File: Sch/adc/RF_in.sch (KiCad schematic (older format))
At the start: 72 parts, among them CN1 SMA, CN2 SMA, J3 JP2, J4 JP2, U1 LTC2292, U2 BGA2818

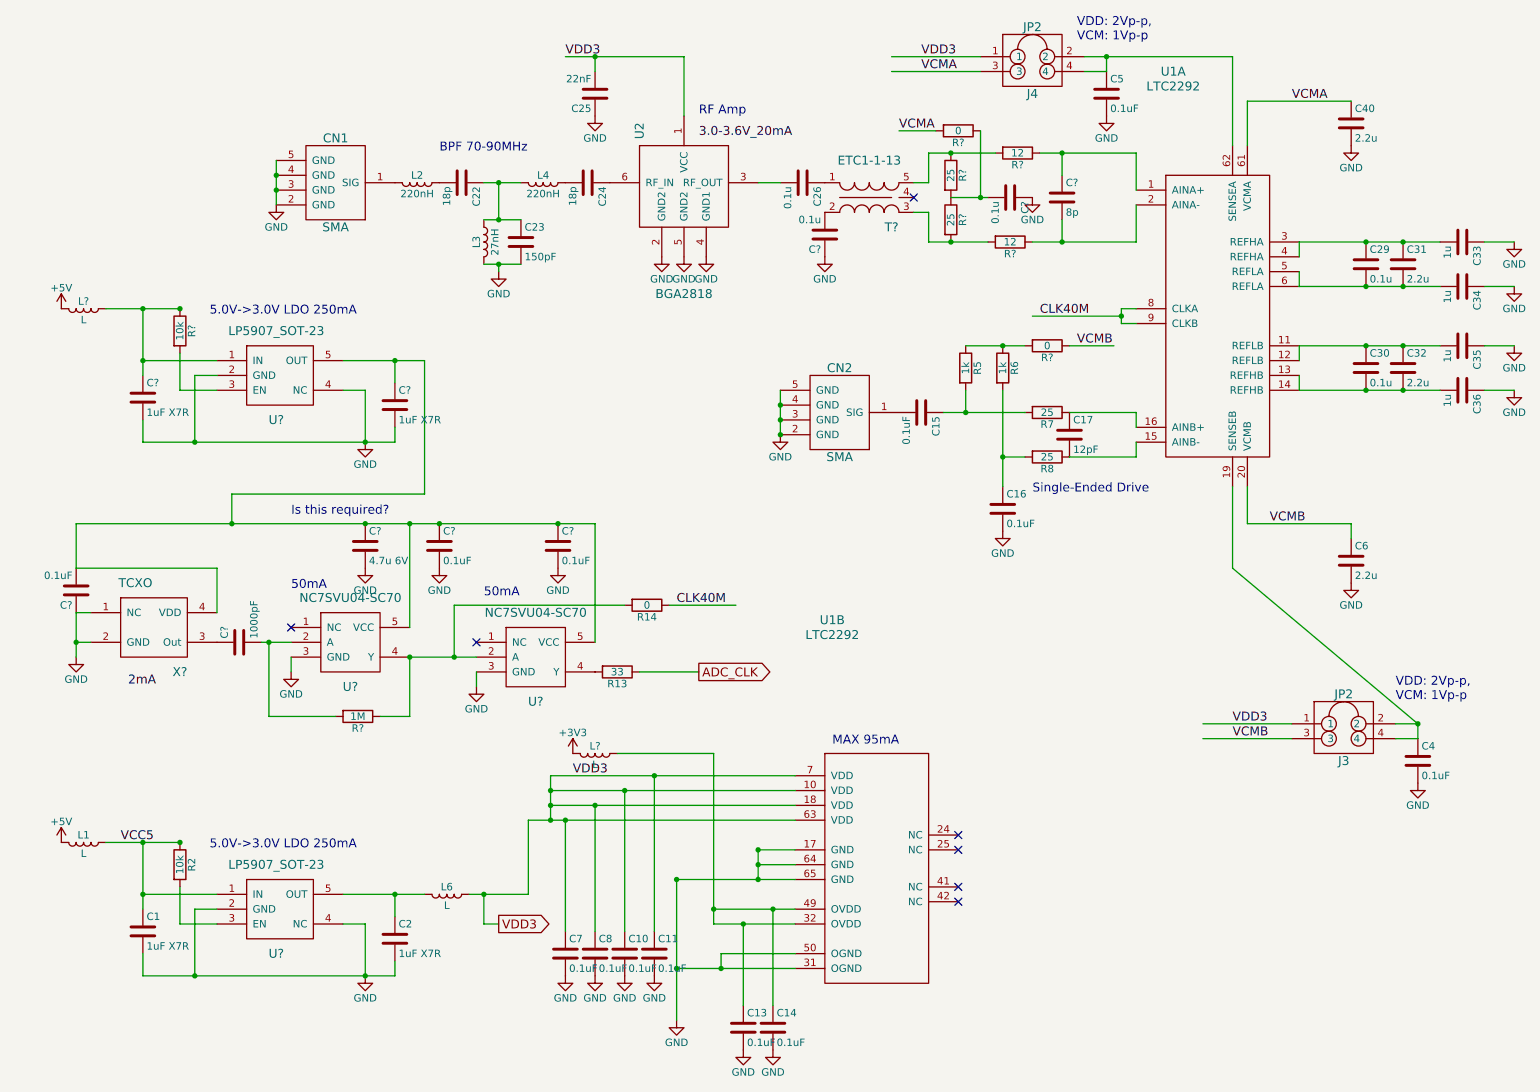
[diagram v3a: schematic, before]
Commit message: Analog front end is removed from the ADC board. ADC board is done
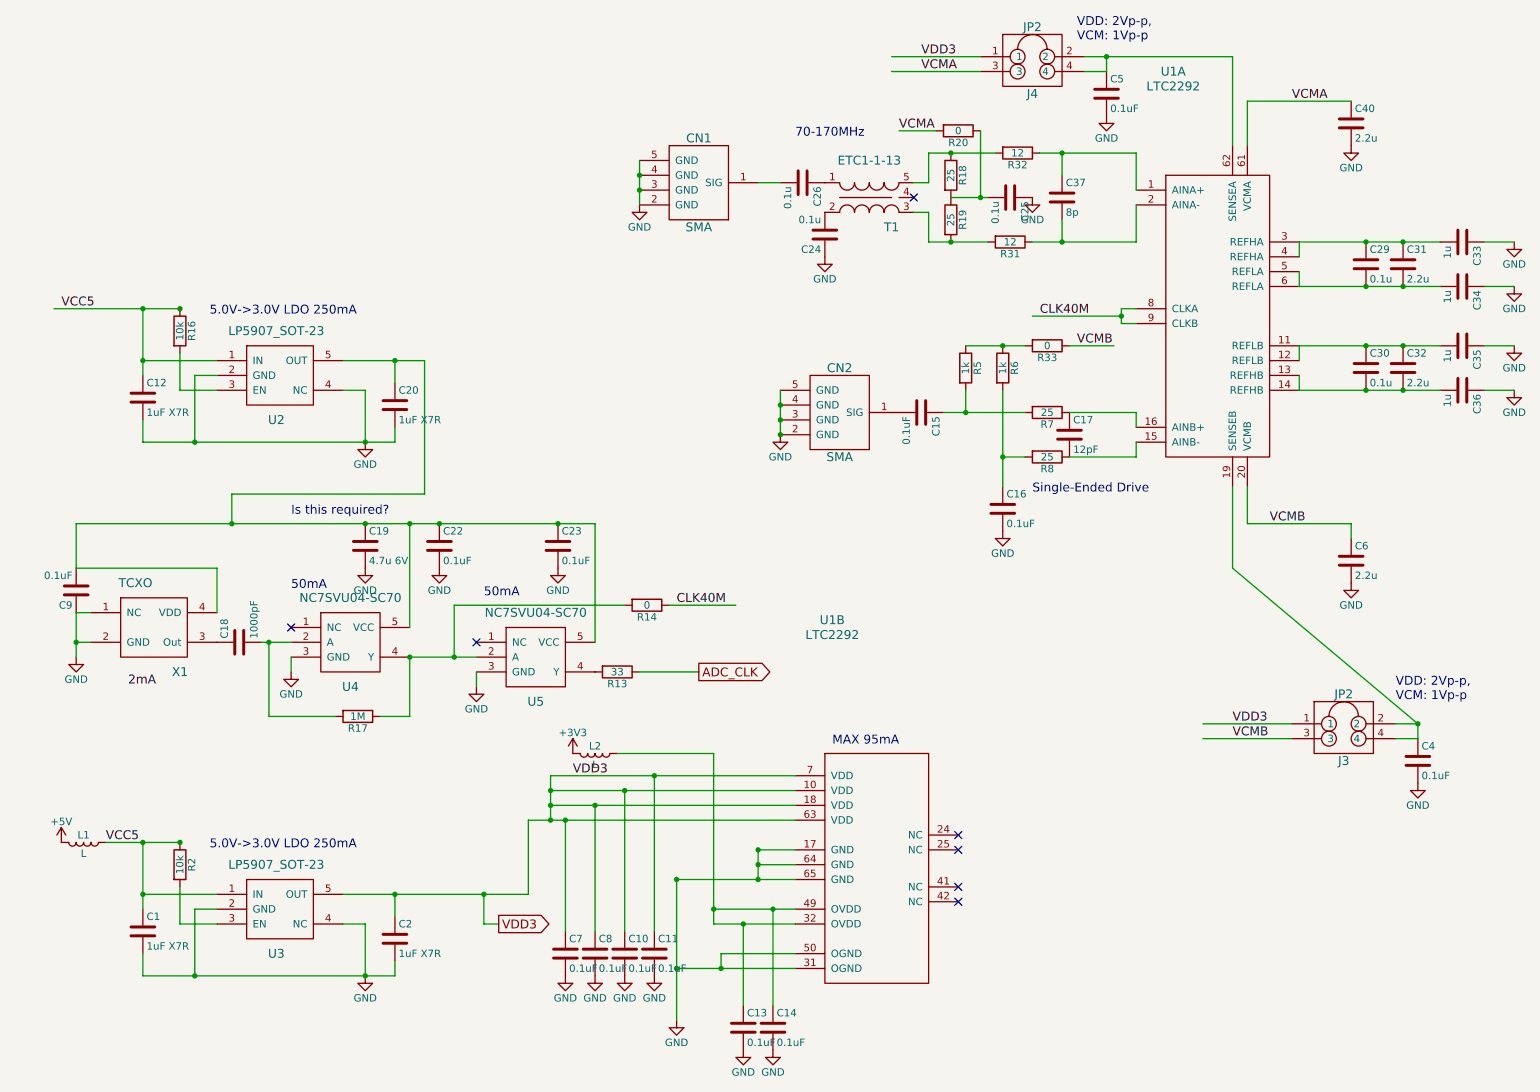
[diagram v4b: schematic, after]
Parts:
- removed C22, C24: 18p, adc_lib:C0603, symbol C
- removed C23: 150pF, adc_lib:C0603, symbol C
- removed C25: 22nF, adc_lib:C0603, symbol C
- removed L2, L4: 220nH, adc_lib:L0603, symbol L
- removed L3: 27nH, adc_lib:L0603, symbol L
- removed L6, L?: L, adc_lib:FB0805, symbol L
- removed U2: BGA2818, adc_lib:BGA2818, symbol BGA2818
- gave numbers to parts that had none: 25
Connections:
- net labels removed: 3.0-3.6V_20mA
- wire segments 149 -> 140
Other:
- note added: "70-170MHz"
- note removed: "BPF 70-90MHz"
- note removed: "RF Amp"
- moved on the sheet: CN1
